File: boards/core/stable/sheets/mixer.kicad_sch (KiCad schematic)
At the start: 21 parts, among them U208 TL072

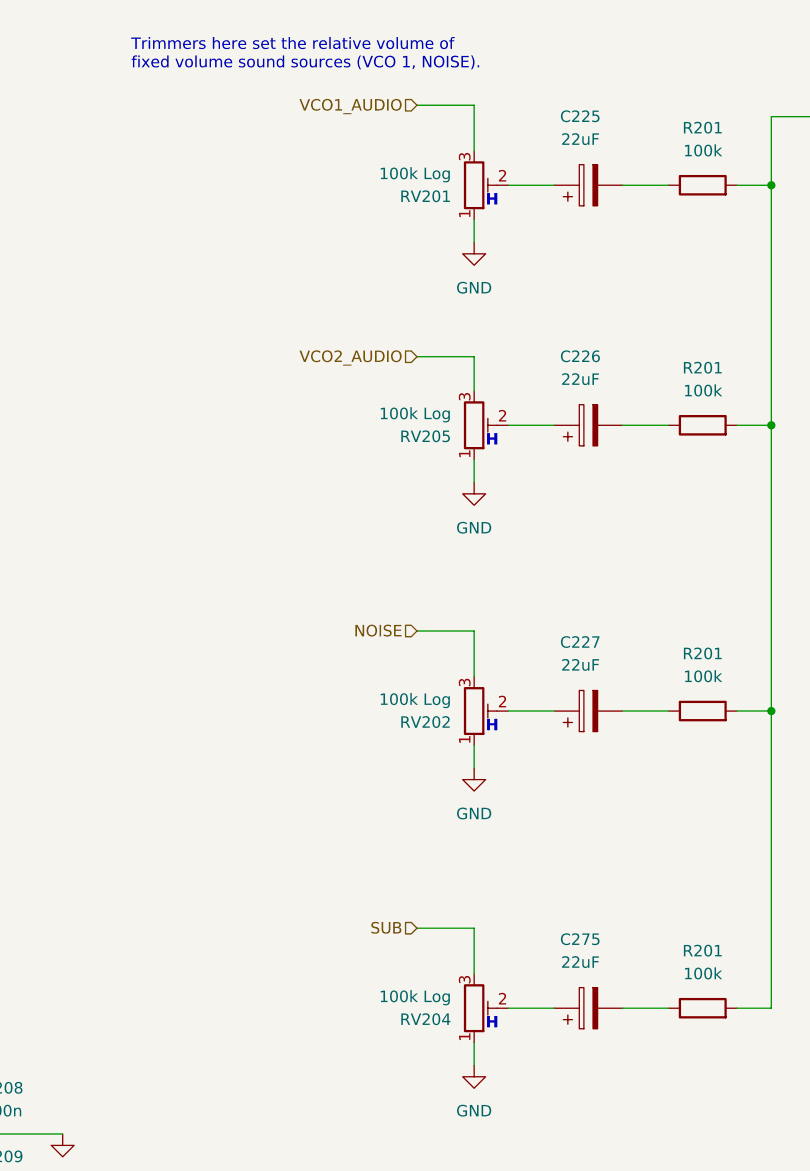
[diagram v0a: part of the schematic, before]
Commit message: Updated and checked Core board BOM
ref https://github.com/shmoergh/hog/issues/19
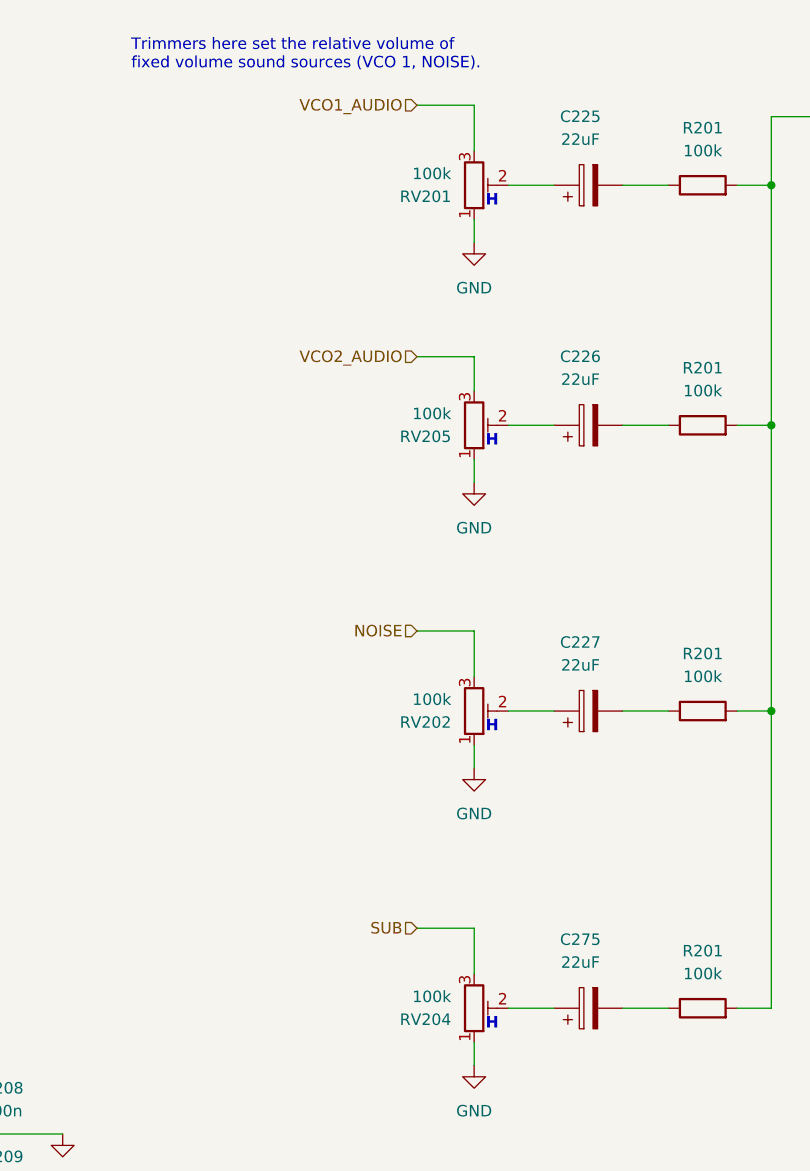
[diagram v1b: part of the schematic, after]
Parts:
- C208, C209, R201, R245, U208: Vendor (none) -> JLCPCB
- C225, C226, C227, C275: Vendor (none) -> JLCPCB; now in the parts list
- RV201, RV202, RV204, RV205: value 100k Log -> 100k; Part No. (none) -> 531-PT6KH104A1010PM; Part URL (none) -> https://mou.sr/49zQlIS; Vendor (none) -> Mouser; now in the parts list

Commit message: Added JLCPCB production files to Core
ref https://github.com/shmoergh/hog/issues/19
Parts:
- C225, C226, C227, C275: FT Rotation Offset (none) -> 180; LCSC C3001241 -> C2836438
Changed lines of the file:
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@@
 			)
 		)
-		(property "LCSC" "C3001241"
+		(property "LCSC" "C2836438"
 			(at 102.87 163.83 90)
 			(effects
@@
 		(property "Vendor" "JLCPCB"
 			(at 102.87 163.83 0)
+			(effects
+				(font
+					(size 1.27 1.27)
+				)
+				(hide yes)
+			)
+		)
+		(property "FT Rotation Offset" "180"
+			(at 102.87 163.83 90)
 			(effects
 				(font
@@
 			)
 		)
-		(property "LCSC" "C3001241"
+		(property "LCSC" "C2836438"
 			(at 102.87 99.06 90)
 			(effects
@@
 		(property "Vendor" "JLCPCB"
 			(at 102.87 99.06 0)
+			(effects
+				(font
+					(size 1.27 1.27)
+				)
+				(hide yes)
+			)
+		)
+		(property "FT Rotation Offset" "180"
+			(at 102.87 99.06 90)
 			(effects
 				(font
@@
 			)
 		)
-		(property "LCSC" "C3001241"
+		(property "LCSC" "C2836438"
 			(at 102.87 72.39 90)
 			(effects
@@
 		(property "Vendor" "JLCPCB"
 			(at 102.87 72.39 0)
+			(effects
+				(font
+					(size 1.27 1.27)
+				)
+				(hide yes)
+			)
+		)
+		(property "FT Rotation Offset" "180"
+			(at 102.87 72.39 90)
 			(effects
 				(font
@@
 			)
 		)
-		(property "LCSC" "C3001241"
+		(property "LCSC" "C2836438"
 			(at 102.87 130.81 90)
 			(effects
@@
 			(effects
 				(font
+					(size 1.27 1.27)
+				)
+				(hide yes)
+			)
+		)
+		(property "FT Rotation Offset" "180"
+			(at 102.87 130.81 90)
+			(effects
+				(font
